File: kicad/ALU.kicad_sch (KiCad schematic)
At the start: 8 parts, among them U1 MC14008BDR2G, U2 MC14008BDR2G, U3 74HC86, U4 74HC86, U5 74HC86, U6 74HC86, U7 74HC86

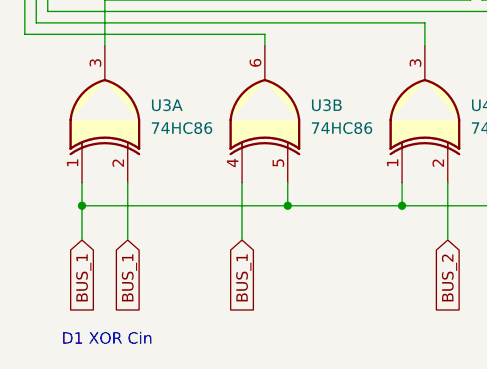
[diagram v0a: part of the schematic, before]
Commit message: update schematic
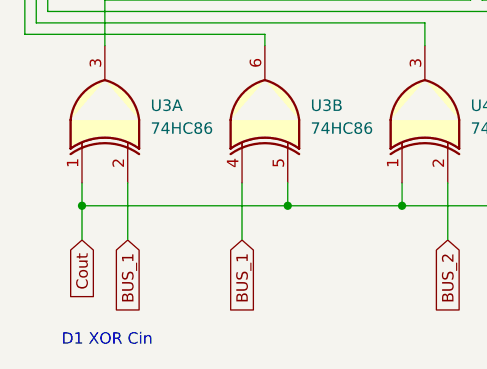
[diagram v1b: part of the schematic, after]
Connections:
- net BUS_1: no longer U3.1, U3.5, U4.1, U4.5, U5.1, U5.5, U6.1, U6.5, U7.5
- new net Cout: U3.1, U3.5, U4.1, U4.5, U5.1, U5.5, U6.1, U6.5, U7.5
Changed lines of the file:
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@@
 		)
 	)
-	(global_label "BUS_1"
+	(global_label "Cout"
 		(shape input)
 		(at 82.55 137.16 270)
@@
 		)
 		(property "Intersheetrefs" "${INTERSHEET_REFS}"
-			(at 82.55 146.1323 90)
+			(at 82.55 144.4389 90)
 			(effects
 				(font

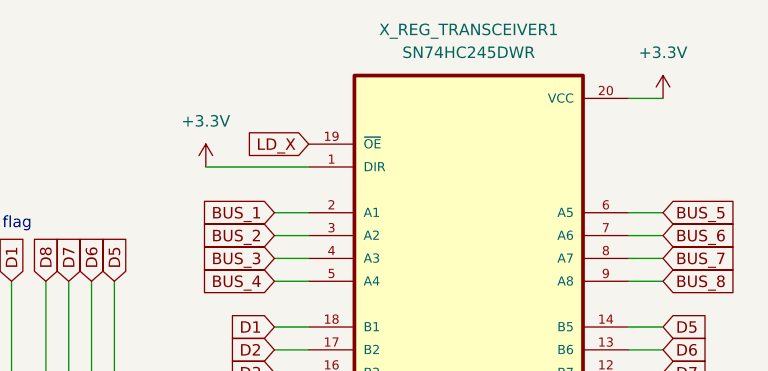
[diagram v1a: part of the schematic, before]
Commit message: update schematic
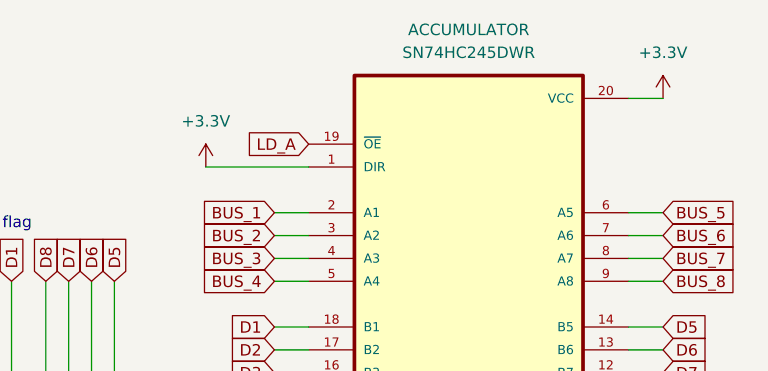
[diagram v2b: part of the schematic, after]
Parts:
- renumbered X_REG_TRANSCEIVER1 to ACCUMULATOR
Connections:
- net LD_X renamed LD_A
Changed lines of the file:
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@@
 		)
 	)
-	(global_label "LD_X"
+	(global_label "LD_A"
 		(shape input)
 		(at 217.17 48.26 180)
@@
 		)
 		(property "Intersheetrefs" "${INTERSHEET_REFS}"
-			(at 209.7096 48.26 0)
+			(at 209.8305 48.26 0)
 			(effects
 				(font
@@
 		(dnp no)
 		(fields_autoplaced yes)
-		(property "Reference" "X_REG_TRANSCEIVER1"
+		(property "Reference" "ACCUMULATOR"
 			(at 234.95 35.56 0)
 			(effects
@@
 			(project "my_computer"
 				(path "/d90612be-a4bb-4b59-8bc6-93e31ea1f515/302200b6-361c-456d-bc2e-53c1b83aa47a"
-					(reference "X_REG_TRANSCEIVER1")
+					(reference "ACCUMULATOR")
 					(unit 1)
 				)

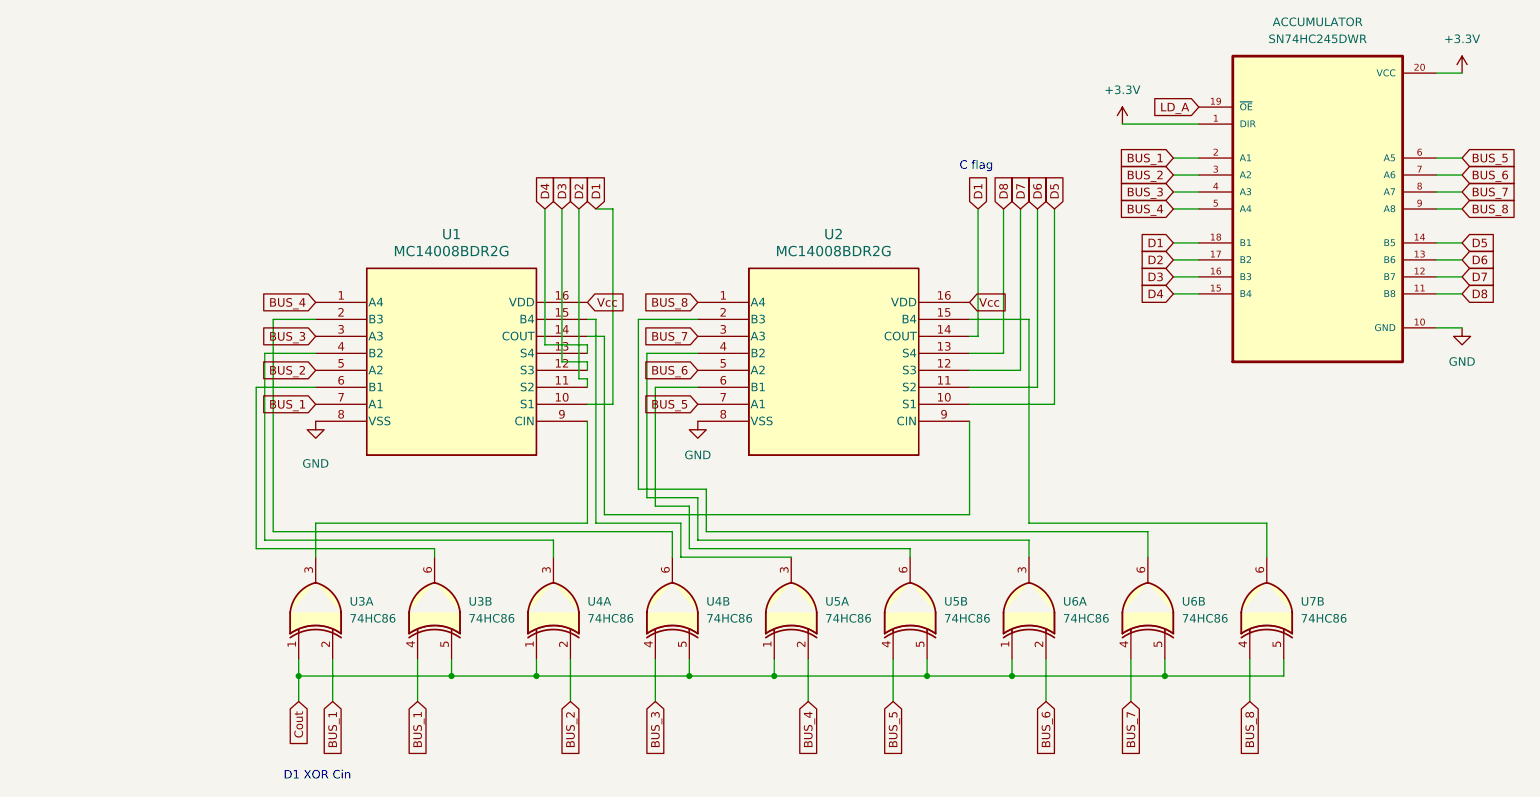
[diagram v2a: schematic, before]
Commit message: update schematic
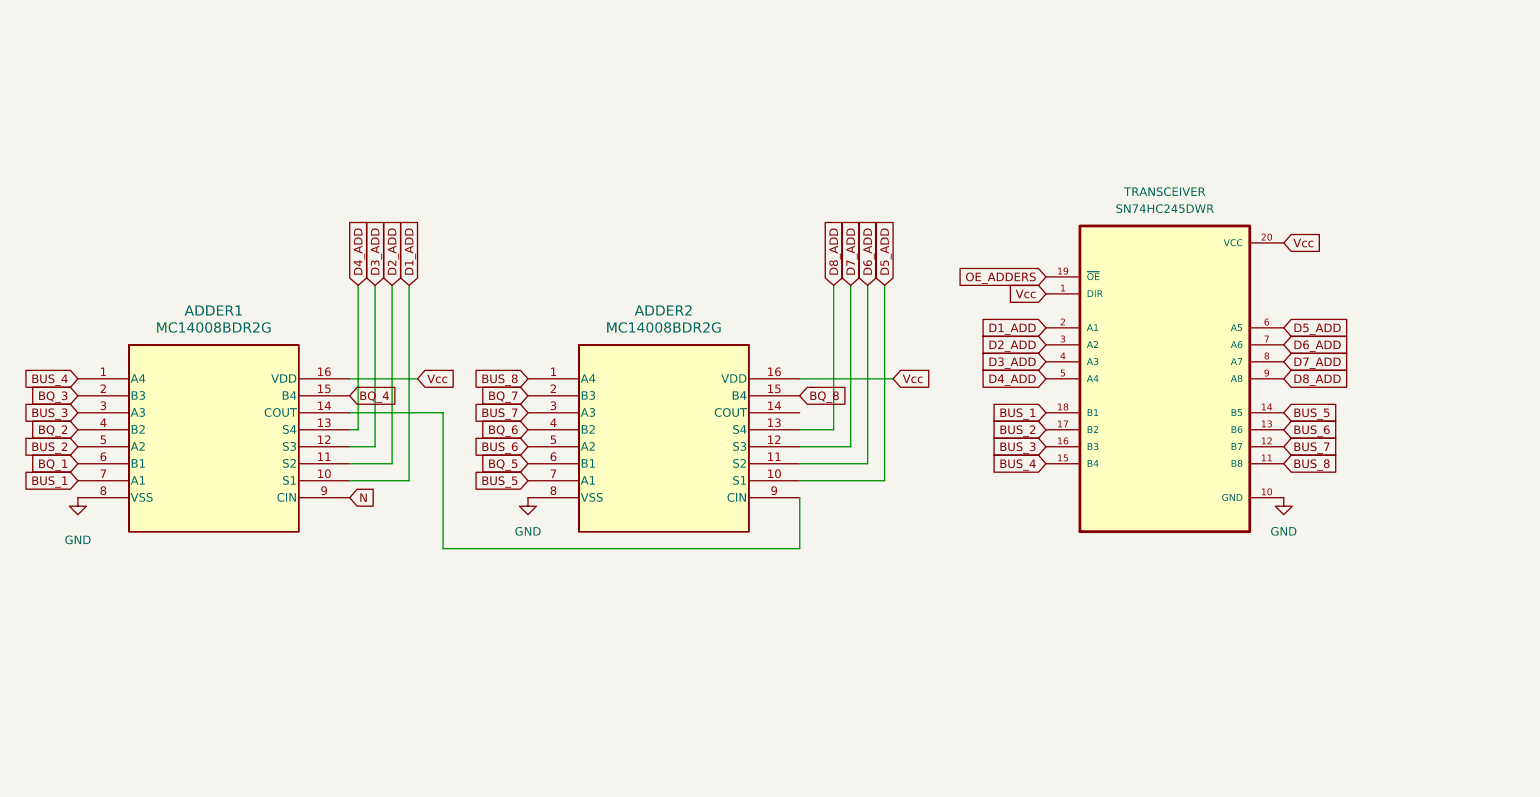
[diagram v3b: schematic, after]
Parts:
- removed U3, U4, U5, U6, U7: 74HC86, symbol 74xx:74HC86
- renumbered U1 to ADDER1, U2 to ADDER2, ACCUMULATOR to TRANSCEIVER
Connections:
- net +3.3V is gone; now on net Vcc: TRANSCEIVER.1 (DIR), TRANSCEIVER.20 (VCC)
- net BUS_1: now also TRANSCEIVER.18 (B1); no longer TRANSCEIVER.2 (A1)
- net BUS_2: now also TRANSCEIVER.17 (B2); no longer TRANSCEIVER.3 (A2)
- net BUS_3: now also TRANSCEIVER.16 (B3); no longer TRANSCEIVER.4 (A3)
- net BUS_4: now also TRANSCEIVER.15 (B4); no longer TRANSCEIVER.5 (A4)
- net BUS_5: now also TRANSCEIVER.14 (B5); no longer TRANSCEIVER.6 (A5)
- net BUS_6: now also TRANSCEIVER.13 (B6); no longer TRANSCEIVER.7 (A6)
- net BUS_7: now also TRANSCEIVER.12 (B7); no longer TRANSCEIVER.8 (A7)
- net BUS_8: now also TRANSCEIVER.11 (B8); no longer TRANSCEIVER.9 (A8)
- net BQ_4: now reaches ADDER1.15 (B4)
- net BQ_3: now reaches ADDER1.2 (B3)
- net BQ_2: now reaches ADDER1.4 (B2)
- net BQ_1: now reaches ADDER1.6 (B1)
- net N: now reaches ADDER1.9 (CIN)
- net BQ_8: now reaches ADDER2.15 (B4)
- net BQ_7: now reaches ADDER2.2 (B3)
- net BQ_6: now reaches ADDER2.4 (B2)
- net BQ_5: now reaches ADDER2.6 (B1)
- removed net D1: ADDER1.10 (S1), ADDER2.14 (COUT), TRANSCEIVER.18 (B1)
- net D2 renamed D2_ADD
- net D2_ADD: now also TRANSCEIVER.3 (A2); no longer TRANSCEIVER.17 (B2)
- net D3 renamed D3_ADD
- net D3_ADD: now also TRANSCEIVER.4 (A3); no longer TRANSCEIVER.16 (B3)
- net D4 renamed D4_ADD
- net D4_ADD: now also TRANSCEIVER.5 (A4); no longer TRANSCEIVER.15 (B4)
- net D5 renamed D5_ADD
- net D5_ADD: now also TRANSCEIVER.6 (A5); no longer TRANSCEIVER.14 (B5)
- net D6 renamed D6_ADD
- net D6_ADD: now also TRANSCEIVER.7 (A6); no longer TRANSCEIVER.13 (B6)
- net D7 renamed D7_ADD
- net D7_ADD: now also TRANSCEIVER.8 (A7); no longer TRANSCEIVER.12 (B7)
- net D8 renamed D8_ADD
- net D8_ADD: now also TRANSCEIVER.9 (A8); no longer TRANSCEIVER.11 (B8)
- net LD_A renamed OE_ADDERS
- new net D1_ADD: ADDER1.10 (S1), TRANSCEIVER.2 (A1)
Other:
- note removed: "C flag"
- note removed: "D1 XOR Cin"
- moved on the sheet: ADDER1, ADDER2, TRANSCEIVER
